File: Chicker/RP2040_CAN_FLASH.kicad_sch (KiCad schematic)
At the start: 66 parts, among them J1 JST_B3B-XH-A, J2 USB4145-03-0170-C_REVA2, J3 JST_BM04B-GHS-TBT, J5 Conn_02x10_Counter_Clockwise, Q1 BSS138, Q4 BSS138, U1 RPI2040, U10 PTS647SM38SMTR2LFS, U5 W25Q16JVSNIQ, U6 SN65HVD233, U7 MCP2515-xST, U9 PTS647SM38SMTR2LFS, Y1 ABM3-12.000MHZ-D2Y-T, Y2 ABM3-8.000MHZ-D2Y-T

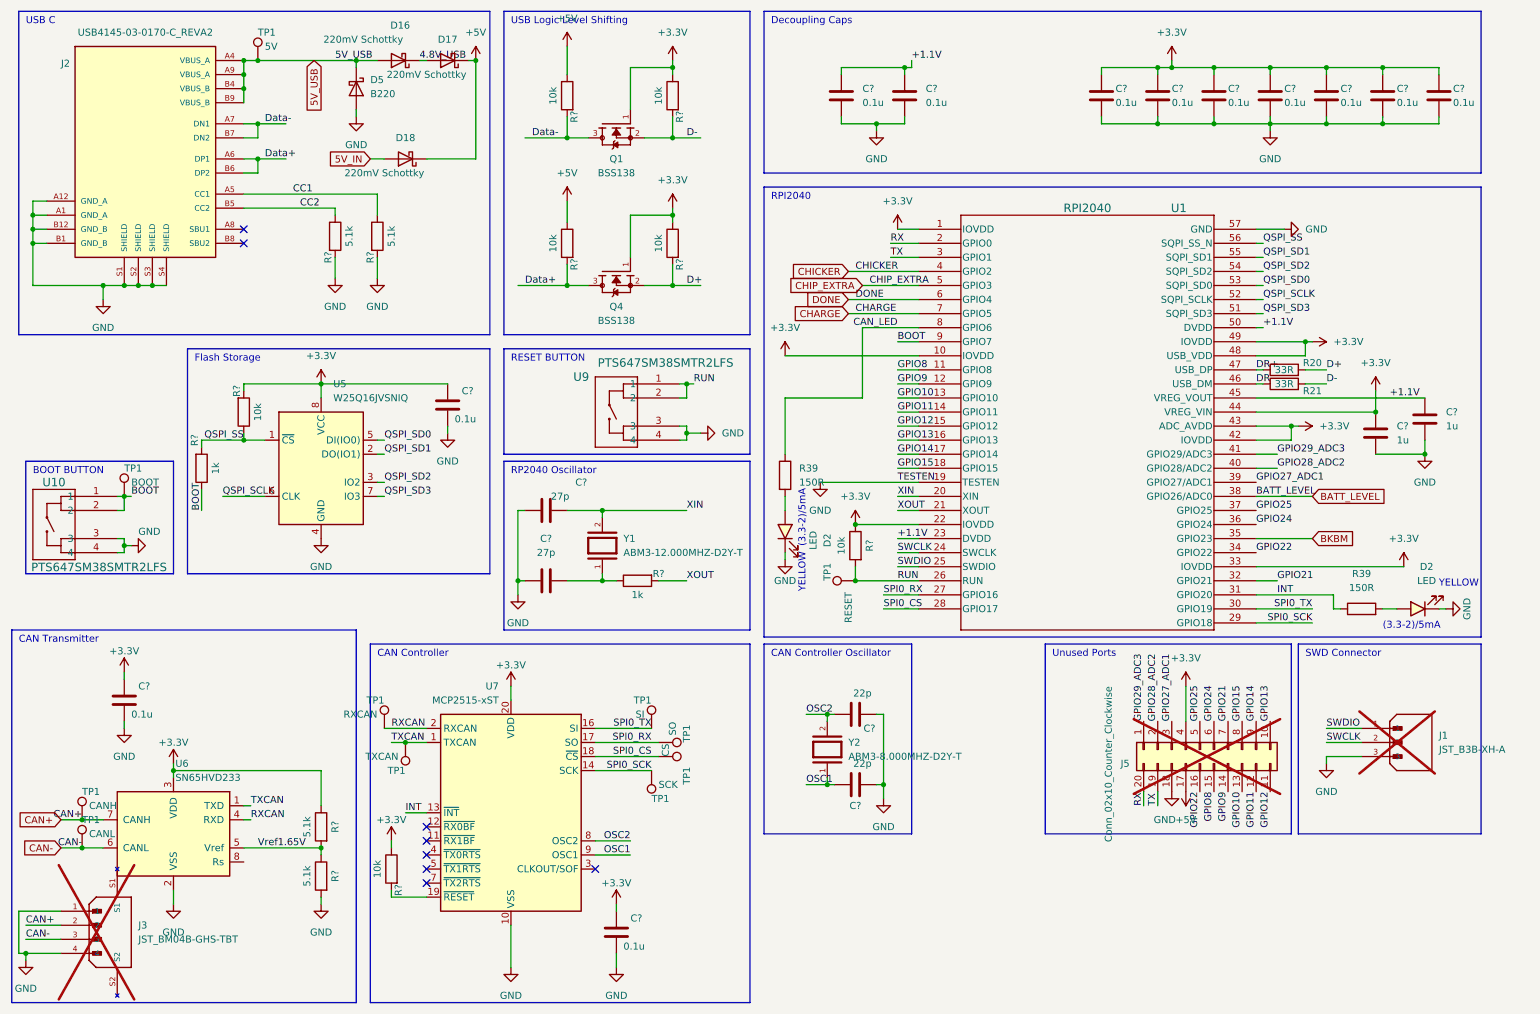
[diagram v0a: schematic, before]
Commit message: update to schematic but something on layout is broken
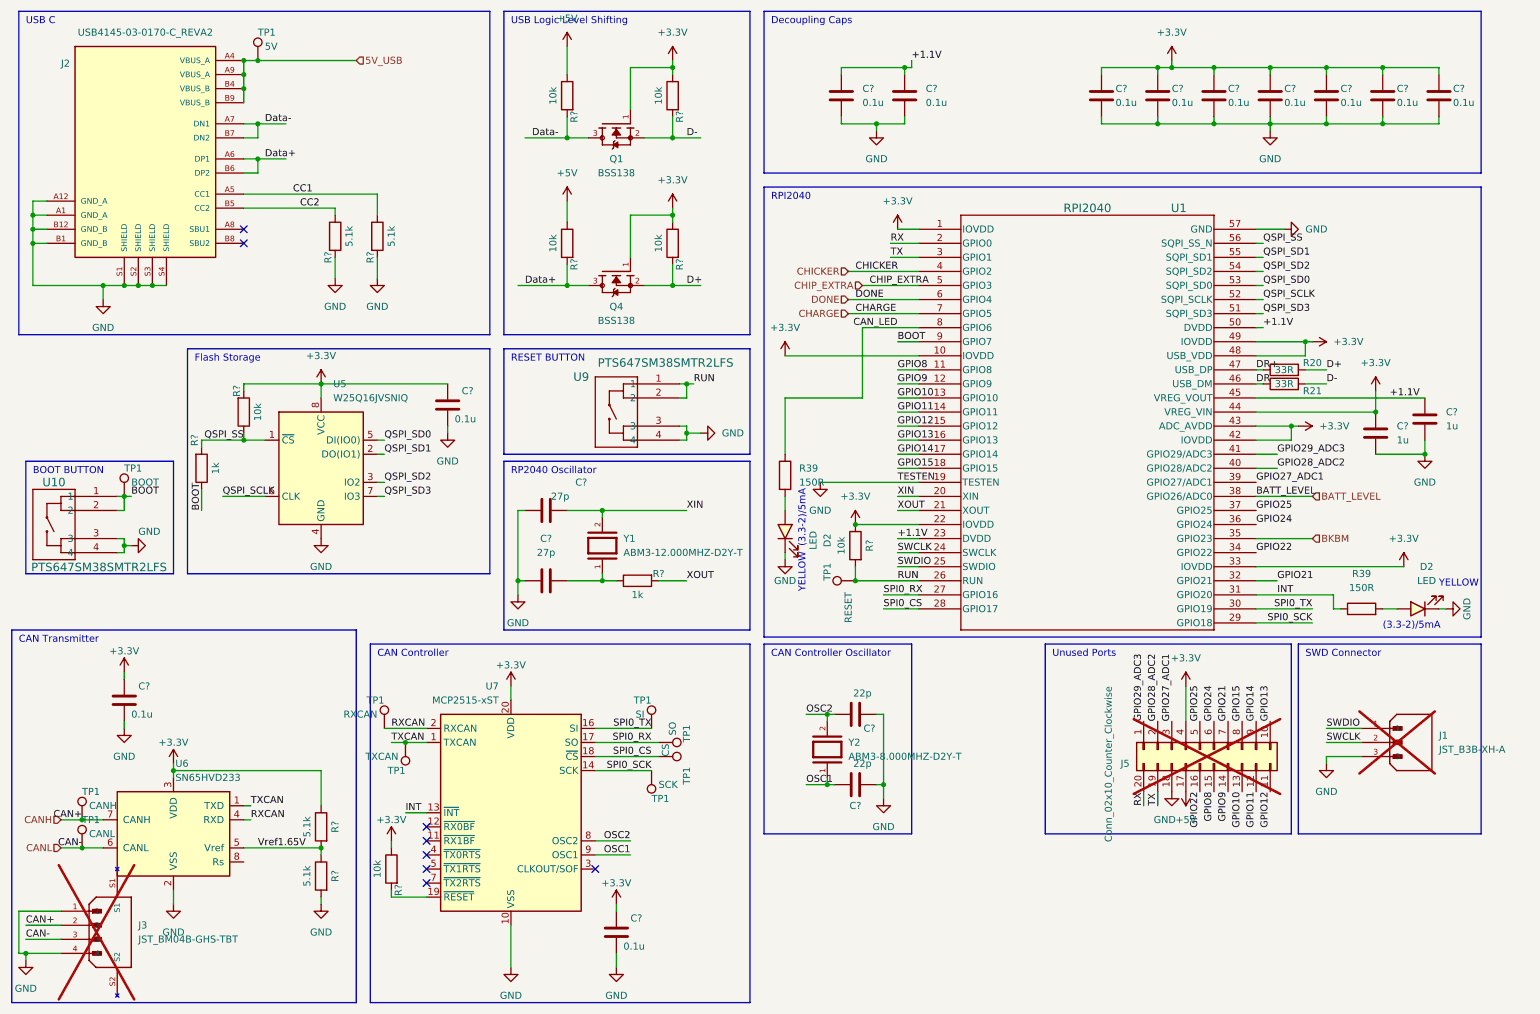
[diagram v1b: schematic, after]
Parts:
- removed D16, D17, D18: 220mV Schottky, bots:D_SOD-323_HandSoldering, symbol bots:D_CUS08F30,H3F
- removed D5: B220, bots:D_SMB, symbol bots:B220
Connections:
- net CAN+ renamed CANH
- net CAN- renamed CANL

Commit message: midplate 4 layers, chicker shell off limit switch idea
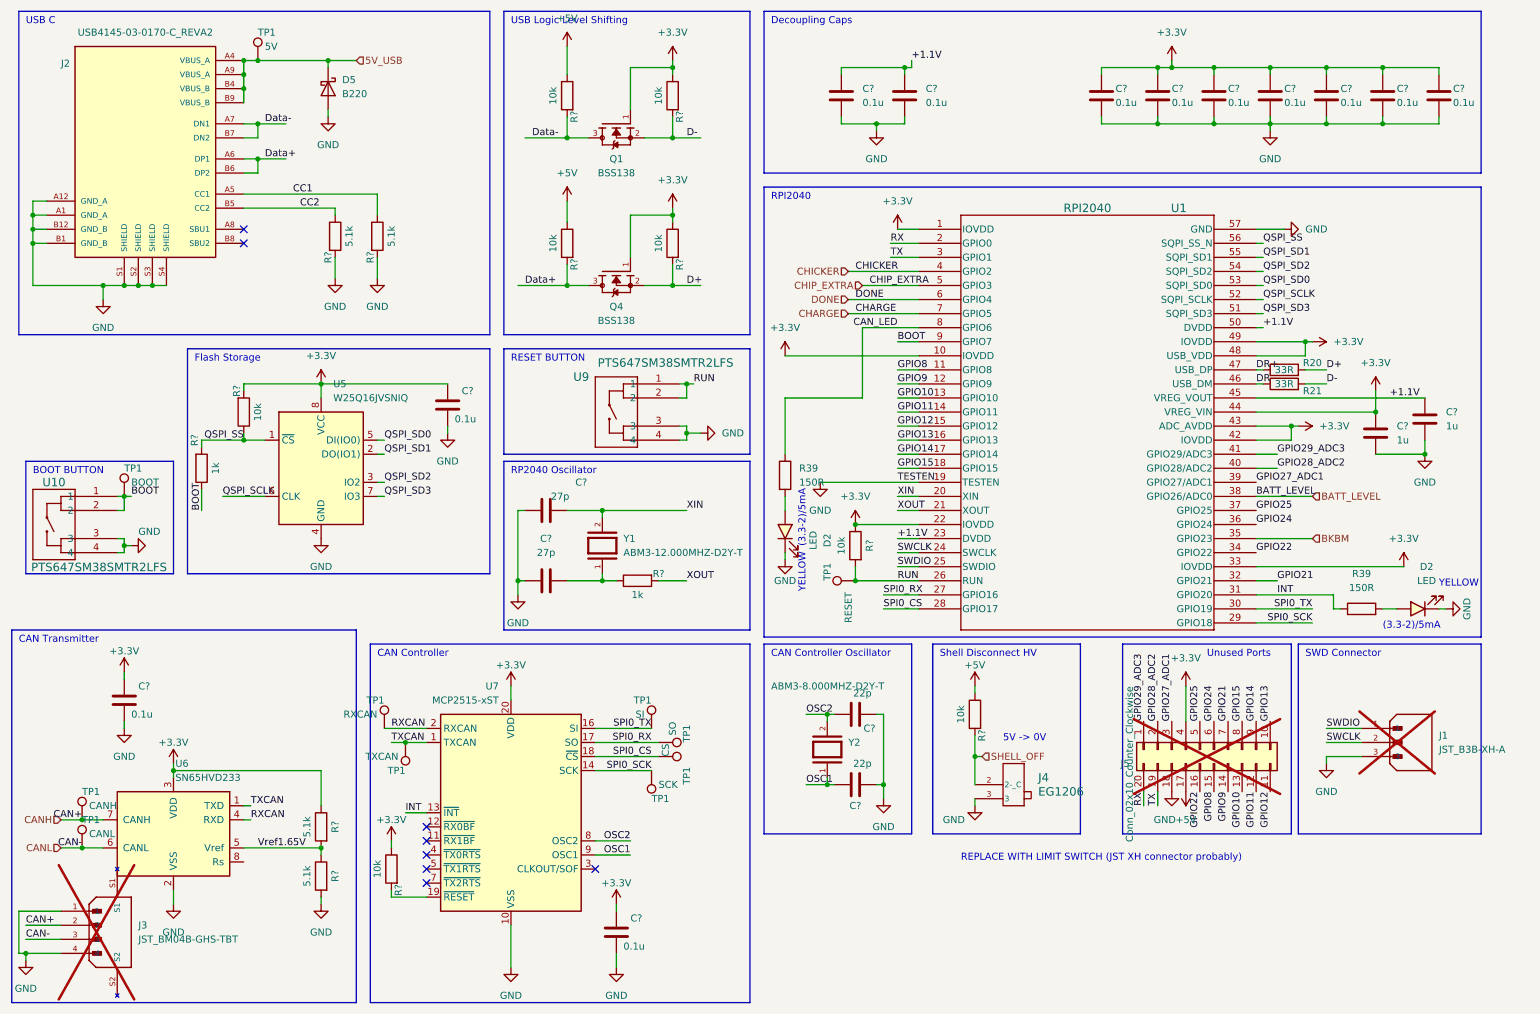
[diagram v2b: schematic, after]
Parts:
- added D5: B220, bots:D_SMB, symbol bots:B220
- added J4: EG1206, bots:SW_EG1206, symbol bots:SW_EG1206
- added R?: 10k, bots:R_0603_1608Metric, symbol bots:R_10k
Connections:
- net +5V: now also R?.1
- net 5V_USB: now also D5.1 (K)
- net GND: now also D5.2 (A), J4.3
- new net SHELL_OFF: J4.2 (2-_C), R?.2
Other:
- note added: "5V -> 0V"
- note added: "REPLACE WITH LIMIT SWITCH (JST XH connector probably)"
- note added: "Shell Disconnect HV"

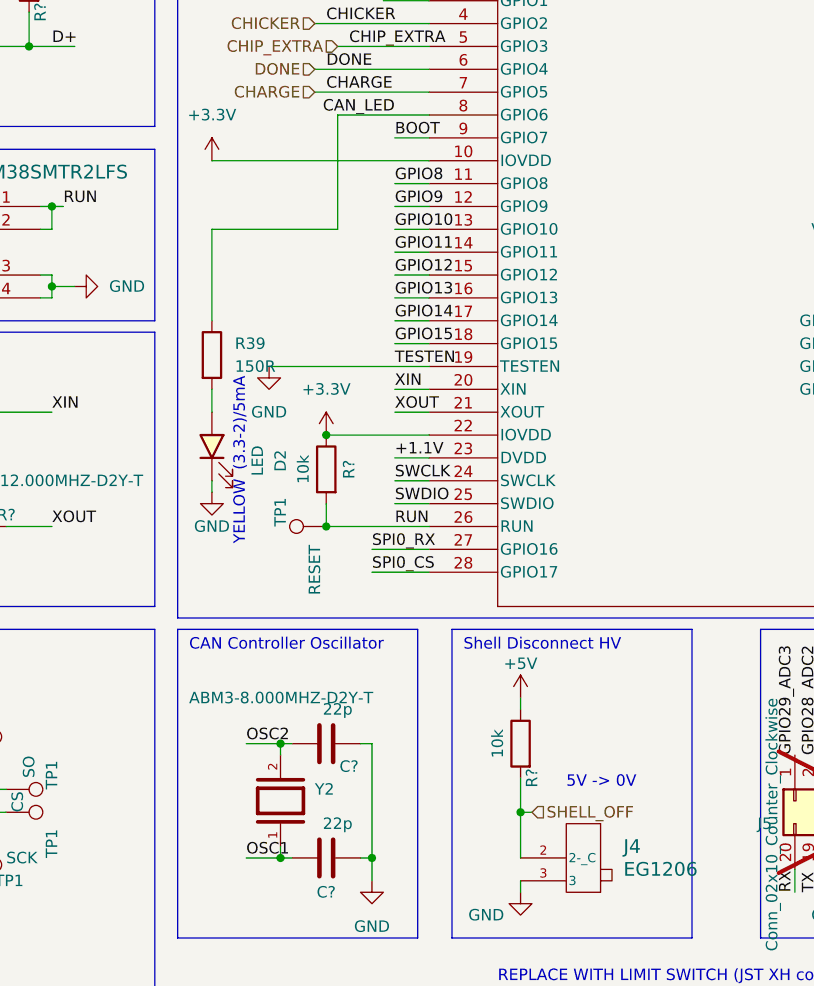
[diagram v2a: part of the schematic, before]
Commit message: chicker discharge HV shell off fixed
pull up to 3v3 and limit switch, input to RP2040, output to inverted discharge signal which discharges if it is set to 0
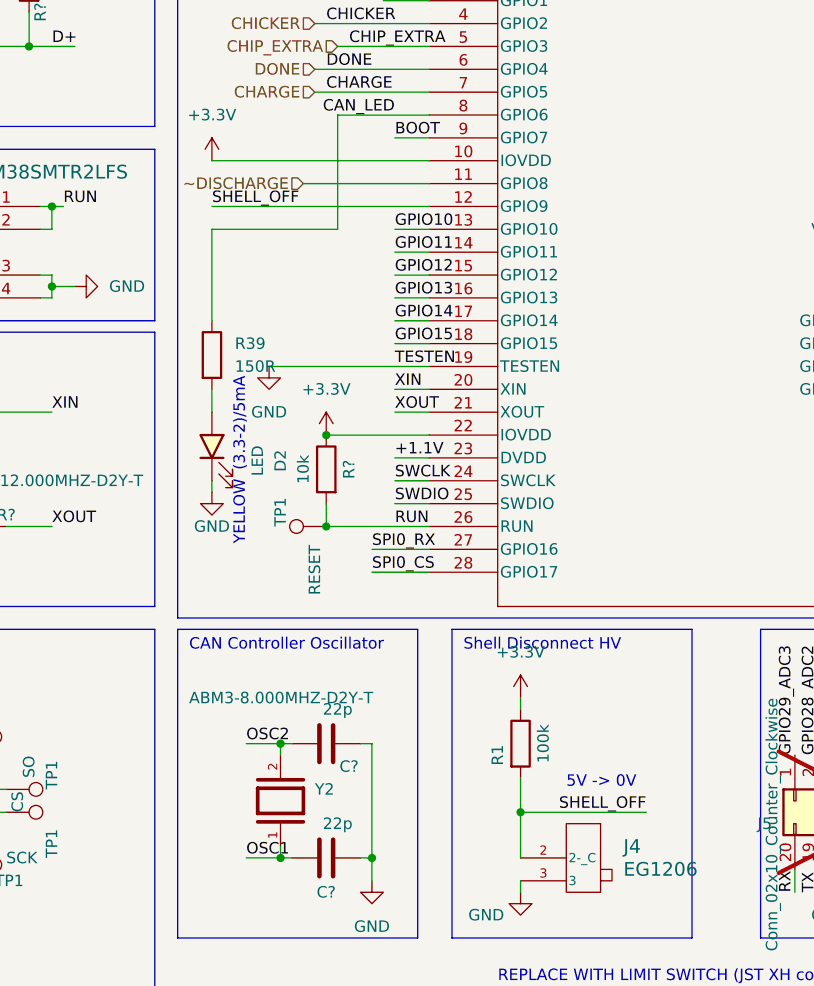
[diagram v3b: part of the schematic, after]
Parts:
- removed R?: 10k, bots:R_0603_1608Metric, symbol bots:R_10k
- added R1: 100k, bots:R_0603_1608Metric, symbol bots:R_100k
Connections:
- net +3.3V: now also R1.1
- net GPIO8: no longer U1.11 (GPIO8)
- net GPIO9: no longer U1.12 (GPIO9)
- net SHELL_OFF: now also U1.12 (GPIO9), R1.2
- new net ~DISCHARGE: U1.11 (GPIO8)
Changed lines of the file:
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@@
     (stroke (width 0) (type default))
   )
-  (wire (pts (xy 173.99 82.55) (xy 177.8 82.55))
+  (wire (pts (xy 153.67 82.55) (xy 177.8 82.55))
     (stroke (width 0) (type default))
   )
@@
     (stroke (width 0) (type default))
   )
-  (wire (pts (xy 187.96 149.86) (xy 189.23 149.86))
+  (wire (pts (xy 187.96 149.86) (xy 201.93 149.86))
     (stroke (width 0) (type default))
   )
@@
     (stroke (width 0) (type default))
   )
-  (wire (pts (xy 173.99 80.01) (xy 177.8 80.01))
+  (wire (pts (xy 163.83 80.01) (xy 177.8 80.01))
     (stroke (width 0) (type default))
   )
@@
     (effects (font (size 1.27 1.27)) (justify left bottom))
   )
+  (label "SHELL_OFF" (at 153.67 82.55 0) (fields_autoplaced)
+    (effects (font (size 1.27 1.27)) (justify left bottom))
+  )
+  (label "SHELL_OFF" (at 201.93 149.86 180) (fields_autoplaced)
+    (effects (font (size 1.27 1.27)) (justify right bottom))
+  )
   (label "QSPI_SCLK" (at 240.03 67.31 0) (fields_autoplaced)
     (effects (font (size 1.27 1.27)) (justify left bottom))
@@
     (effects (font (size 1.27 1.27)) (justify left bottom))
   )
-  (label "GPIO9" (at 173.99 82.55 0) (fields_autoplaced)
-    (effects (font (size 1.27 1.27)) (justify left bottom))
-  )
   (label "GPIO28_ADC2" (at 220.98 143.51 90) (fields_autoplaced)
     (effects (font (size 1.27 1.27)) (justify left bottom))
@@
     (effects (font (size 1.27 1.27)) (justify left bottom))
   )
-  (label "GPIO8" (at 173.99 80.01 0) (fields_autoplaced)
-    (effects (font (size 1.27 1.27)) (justify left bottom))
-  )
   (label "SPI0_SCK" (at 129.54 152.4 180) (fields_autoplaced)
     (effects (font (size 1.27 1.27)) (justify right bottom))
@@
     (effects (font (size 1.27 1.27)) (justify right))
   )
-  (hierarchical_label "SHELL_OFF" (shape input) (at 189.23 149.86 0) (fields_autoplaced)
-    (effects (font (size 1.27 1.27)) (justify left))
+  (hierarchical_label "~DISCHARGE" (shape input) (at 163.83 80.01 180) (fields_autoplaced)
+    (effects (font (size 1.27 1.27)) (justify right))
   )
   (hierarchical_label "CANL" (shape input) (at 22.86 166.37 180) (fields_autoplaced)
@@
     )
   )
+  (symbol (lib_name "R_100k_3") (lib_id "bots:R_100k") (at 187.96 142.24 0) (unit 1)
+    (in_bom yes) (on_board yes) (dnp no)
+    (property "Reference" "R1" (at 185.42 143.51 90)
+      (effects (font (size 1.27 1.27)))
+    )
+    (property "Value" "100k" (at 190.5 142.24 90)
+      (effects (font (size 1.27 1.27)))
+    )
+    (property "Footprint" "bots:R_0603_1608Metric" (at 186.182 142.24 90)
+      (effects (font (size 1.27 1.27)) hide)
+    )
+    (property "Datasheet" "~" (at 187.96 142.24 0)
+      (effects (font (size 1.27 1.27)) hide)
+    )
+    (property "MPN" "0603WAF1003T5E" (at 187.96 142.24 0)
+      (effects (font (size 1.27 1.27)) hide)
+    )
+    (property "Manufacturer" "UNI-ROYAL(Uniroyal Elec)" (at 187.96 142.24 0)
+      (effects (font (size 1.27 1.27)) hide)
+    )
+    (property "Price" "0.0009" (at 187.96 142.24 0)
+      (effects (font (size 1.27 1.27)) hide)
+    )
+    (property "JLC" "0603" (at 187.96 142.24 0)
+      (effects (font (size 1.27 1.27)) hide)
+    )
+    (property "LCSC" "C25803" (at 187.96 142.24 0)
+      (effects (font (size 1.27 1.27)) hide)
+    )
+    (property "JLC Extended" "no" (at 187.96 142.24 0)
+      (effects (font (size 1.27 1.27)) hide)
+    )
+    (pin "1")
+    (pin "2")
+    (instances
+      (project "chicker"
+        (path "/1a9ce3e8-a091-496c-9c5f-e7b2eb60e275"
+          (reference "R1") (unit 1)
+        )
+        (path "/1a9ce3e8-a091-496c-9c5f-e7b2eb60e275/aa68550e-c35d-4fef-b4e5-f1eb6225215f"
+          (reference "R27") (unit 1)
+        )
+        (path "/1a9ce3e8-a091-496c-9c5f-e7b2eb60e275/44109b35-87db-4b37-b749-86ba1243ffef"
+          (reference "R50") (unit 1)
+        )
+      )
+    )
+  )
   (symbol (lib_id "power:+3.3V") (at 223.52 24.13 0) (unit 1)
     (in_bom yes) (on_board yes) (dnp no) (fields_autoplaced)
@@
     )
   )
+  (symbol (lib_id "power:+3.3V") (at 187.96 137.16 0) (mirror y) (unit 1)
+    (in_bom yes) (on_board yes) (dnp no) (fields_autoplaced)
+    (property "Reference" "#PWR011" (at 187.96 140.97 0)
+      (effects (font (size 1.27 1.27)) hide)
+    )
+    (property "Value" "+3.3V" (at 187.96 132.08 0)
+      (effects (font (size 1.27 1.27)))
+    )
+    (property "Footprint" "" (at 187.96 137.16 0)
+      (effects (font (size 1.27 1.27)) hide)
+    )
+    (property "Datasheet" "" (at 187.96 137.16 0)
+      (effects (font (size 1.27 1.27)) hide)
+    )
+    (pin "1")
+    (instances
+      (project "chicker"
+        (path "/1a9ce3e8-a091-496c-9c5f-e7b2eb60e275/13b16574-f046-4bb6-b573-f06681d59f31"
+          (reference "#PWR011") (unit 1)
+        )
+        (path "/1a9ce3e8-a091-496c-9c5f-e7b2eb60e275/44109b35-87db-4b37-b749-86ba1243ffef"
+          (reference "#PWR081") (unit 1)
+        )
+        (path "/1a9ce3e8-a091-496c-9c5f-e7b2eb60e275/aa68550e-c35d-4fef-b4e5-f1eb6225215f"
+          (reference "#PWR074") (unit 1)
+        )
+      )
+    )
+  )
   (symbol (lib_id "power:+3.3V") (at 104.14 137.16 0) (mirror y) (unit 1)
     (in_bom yes) (on_board yes) (dnp no)
@@
     )
   )
-  (symbol (lib_id "bots:R_10k") (at 187.96 142.24 0) (mirror y) (unit 1)
-    (in_bom yes) (on_board yes) (dnp no)
-    (property "Reference" "R?" (at 189.23 146.05 90)
-      (effects (font (size 1.27 1.27)))
-    )
-    (property "Value" "10k" (at 185.42 142.24 90)
-      (effects (font (size 1.27 1.27)))
-    )
-    (property "Footprint" "bots:R_0603_1608Metric" (at 189.738 142.24 90)
-      (effects (font (size 1.27 1.27)) hide)
-    )
-    (property "Datasheet" "~" (at 187.96 142.24 0)
-      (effects (font (size 1.27 1.27)) hide)
-    )
-    (property "MPN" "0603WAF1002T5E" (at 187.96 142.24 0)
-      (effects (font (size 1.27 1.27)) hide)
-    )
-    (property "Manufacturer" "UNI-ROYAL(Uniroyal Elec)" (at 187.96 142.24 0)
-      (effects (font (size 1.27 1.27)) hide)
-    )
-    (property "Price" "0.0008" (at 187.96 142.24 0)
-      (effects (font (size 1.27 1.27)) hide)
-    )
-    (property "JLC" "0603" (at 187.96 142.24 0)
-      (effects (font (size 1.27 1.27)) hide)
-    )
-    (property "LCSC" "C25804" (at 187.96 142.24 0)
-      (effects (font (size 1.27 1.27)) hide)
-    )
-    (property "JLC Extended" "no" (at 187.96 142.24 0)
-      (effects (font (size 1.27 1.27)) hide)
-    )
-    (pin "1")
-    (pin "2")
-    (instances
-      (project "chicker"
-        (path "/1a9ce3e8-a091-496c-9c5f-e7b2eb60e275"
-          (reference "R?") (unit 1)
-        )
-        (path "/1a9ce3e8-a091-496c-9c5f-e7b2eb60e275/44109b35-87db-4b37-b749-86ba1243ffef"
-          (reference "R50") (unit 1)
-        )
-        (path "/1a9ce3e8-a091-496c-9c5f-e7b2eb60e275/aa68550e-c35d-4fef-b4e5-f1eb6225215f"
-          (reference "R48") (unit 1)
-        )
-      )
-    )
-  )
   (symbol (lib_id "bots:C_0.1u") (at 241.3 30.48 0) (unit 1)
     (in_bom yes) (on_board yes) (dnp no)
@@
         )
       )
-    )
-  )
-  (symbol (lib_id "power:+5V") (at 187.96 137.16 0) (unit 1)
-    (in_bom yes) (on_board yes) (dnp no)
-    (property "Reference" "#PWR070" (at 187.96 140.97 0)
-      (effects (font (size 1.27 1.27)) hide)
-    )
-    (property "Value" "+5V" (at 187.96 133.35 0)
-      (effects (font (size 1.27 1.27)))
-    )
-    (property "Footprint" "" (at 187.96 137.16 0)
-      (effects (font (size 1.27 1.27)) hide)
-    )
-    (property "Datasheet" "" (at 187.96 137.16 0)
-      (effects (font (size 1.27 1.27)) hide)
-    )
-    (pin "1")
-    (instances
-      (project "chicker"
-        (path "/1a9ce3e8-a091-496c-9c5f-e7b2eb60e275/13b16574-f046-4bb6-b573-f06681d59f31"
-          (reference "#PWR070") (unit 1)
-        )
-        (path "/1a9ce3e8-a091-496c-9c5f-e7b2eb60e275/44109b35-87db-4b37-b749-86ba1243ffef"
-          (reference "#PWR081") (unit 1)
-        )
-      )
